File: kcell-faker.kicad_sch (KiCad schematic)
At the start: 22 parts, among them J4 DBG, SW1 BOOT, SW2 RST, SW3 UP, SW4 DOWN, SW5 RANGE, U6 ESP32-S3-MINI-1

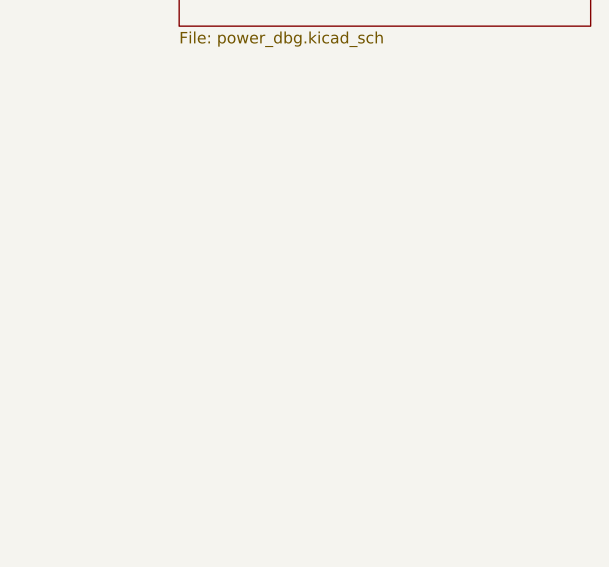
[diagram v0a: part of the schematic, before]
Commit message: Add logos and mounting holes
Straighen up some stuff, align better, untangle transistor outputs
Should we add pins for teh spare channels? we have the ios?
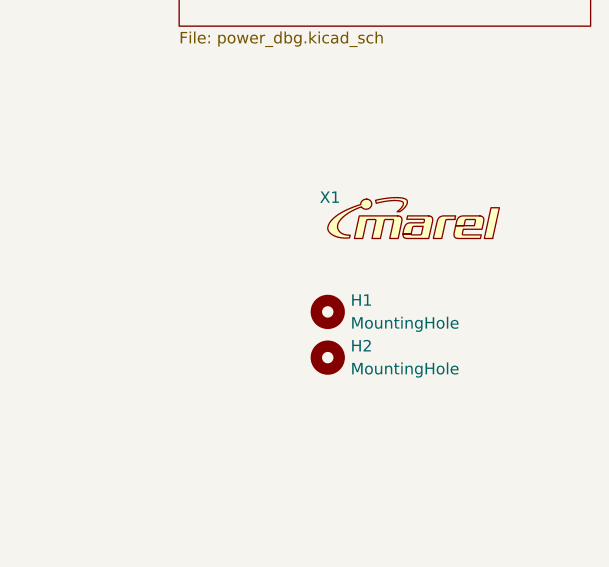
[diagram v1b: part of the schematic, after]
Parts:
- added H1, H2: MountingHole, MountingHole:MountingHole_3.2mm_M3, symbol Mechanical:MountingHole
- added X1: ~, marel-footprints:Logo_Marel_5.3x1.1mm, symbol karl-atomic-basic:Logo_Marel
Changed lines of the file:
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@@
+	)
+	(symbol
+		(lib_id "karl-atomic-basic:Logo_Marel")
+		(at 246.38 129.54 0)
+		(unit 1)
+		(exclude_from_sim no)
+		(in_bom no)
+		(on_board yes)
+		(dnp no)
+		(property "Reference" "X1"
+			(at 246.634 129.54 0)
+			(effects
+				(font
+					(size 1.27 1.27)
+				)
+			)
+		)
+		(property "Value" "~"
+			(at 249.5583 128.27 0)
+			(effects
+				(font
+					(size 1.27 1.27)
+				)
+			)
+		)
+		(property "Footprint" "marel-footprints:Logo_Marel_5.3x1.1mm"
+			(at 246.38 129.54 0)
+			(effects
+				(font
+					(size 1.27 1.27)
+				)
+				(hide yes)
+			)
+		)
+		(property "Datasheet" ""
+			(at 246.38 129.54 0)
+			(effects
+				(font
+					(size 1.27 1.27)
+				)
+				(hide yes)
+			)
+		)
+		(property "Description" ""
+			(at 246.38 129.54 0)
+			(effects
+				(font
+					(size 1.27 1.27)
+				)
+				(hide yes)
+			)
+		)
+		(instances
+			(project ""
+				(path "/dc836b5d-e5fb-485d-8f74-ab331e55e69f"
+					(reference "X1")
+					(unit 1)
+				)
+			)
+		)
 	)
 	(symbol
@@
 	)
 	(symbol
+		(lib_id "Mechanical:MountingHole")
+		(at 246.38 147.32 0)
+		(unit 1)
+		(exclude_from_sim yes)
+		(in_bom no)
+		(on_board yes)
+		(dnp no)
+		(fields_autoplaced yes)
+		(property "Reference" "H2"
+			(at 248.92 146.0499 0)
+			(effects
+				(font
+					(size 1.27 1.27)
+				)
+				(justify left)
+			)
+		)
+		(property "Value" "MountingHole"
+			(at 248.92 148.5899 0)
+			(effects
+				(font
+					(size 1.27 1.27)
+				)
+				(justify left)
+			)
+		)
+		(property "Footprint" "MountingHole:MountingHole_3.2mm_M3"
+			(at 246.38 147.32 0)
+			(effects
+				(font
+					(size 1.27 1.27)
+				)
+				(hide yes)
+			)
+		)
+		(property "Datasheet" "~"
+			(at 246.38 147.32 0)
+			(effects
+				(font
+					(size 1.27 1.27)
+				)
+				(hide yes)
+			)
+		)
+		(property "Description" "Mounting Hole without connection"
+			(at 246.38 147.32 0)
+			(effects
+				(font
+					(size 1.27 1.27)
+				)
+				(hide yes)
+			)
+		)
+		(instances
+			(project "kcell-faker"
+				(path "/dc836b5d-e5fb-485d-8f74-ab331e55e69f"
+					(reference "H2")
+					(unit 1)
+				)
+			)
+		)
+	)
+	(symbol
 		(lib_id "Device:LED_Small")
 		(at 48.26 170.18 90)
@@
 					(unit 1)
 				)
+			)
+		)
+	)
+	(symbol
+		(lib_id "Mechanical:MountingHole")
+		(at 246.38 142.24 0)
+		(unit 1)
+		(exclude_from_sim yes)
+		(in_bom no)
+		(on_board yes)
+		(dnp no)
+		(fields_autoplaced yes)
+		(property "Reference" "H1"
+			(at 248.92 140.9699 0)
+			(effects
+				(font
+					(size 1.27 1.27)
+				)
+				(justify left)
+			)
+		)
+		(property "Value" "MountingHole"
+			(at 248.92 143.5099 0)
+			(effects
+				(font
+					(size 1.27 1.27)
+				)
+				(justify left)
+			)
+		)
+		(property "Footprint" "MountingHole:MountingHole_3.2mm_M3"
+			(at 246.38 142.24 0)
+			(effects
+				(font
+					(size 1.27 1.27)
+				)
+				(hide yes)
+			)
+		)
+		(property "Datasheet" "~"
+			(at 246.38 142.24 0)
+			(effects
+				(font
+					(size 1.27 1.27)
+				)
+				(hide yes)
+			)
+		)
+		(property "Description" "Mounting Hole without connection"
+			(at 246.38 142.24 0)
+			(effects
+				(font
+					(size 1.27 1.27)
+				)
+				(hide yes)
+			)
+		)
+		(instances
+			(project ""
+				(path "/dc836b5d-e5fb-485d-8f74-ab331e55e69f"
+					(reference "H1")
+					(unit 1)
+				)

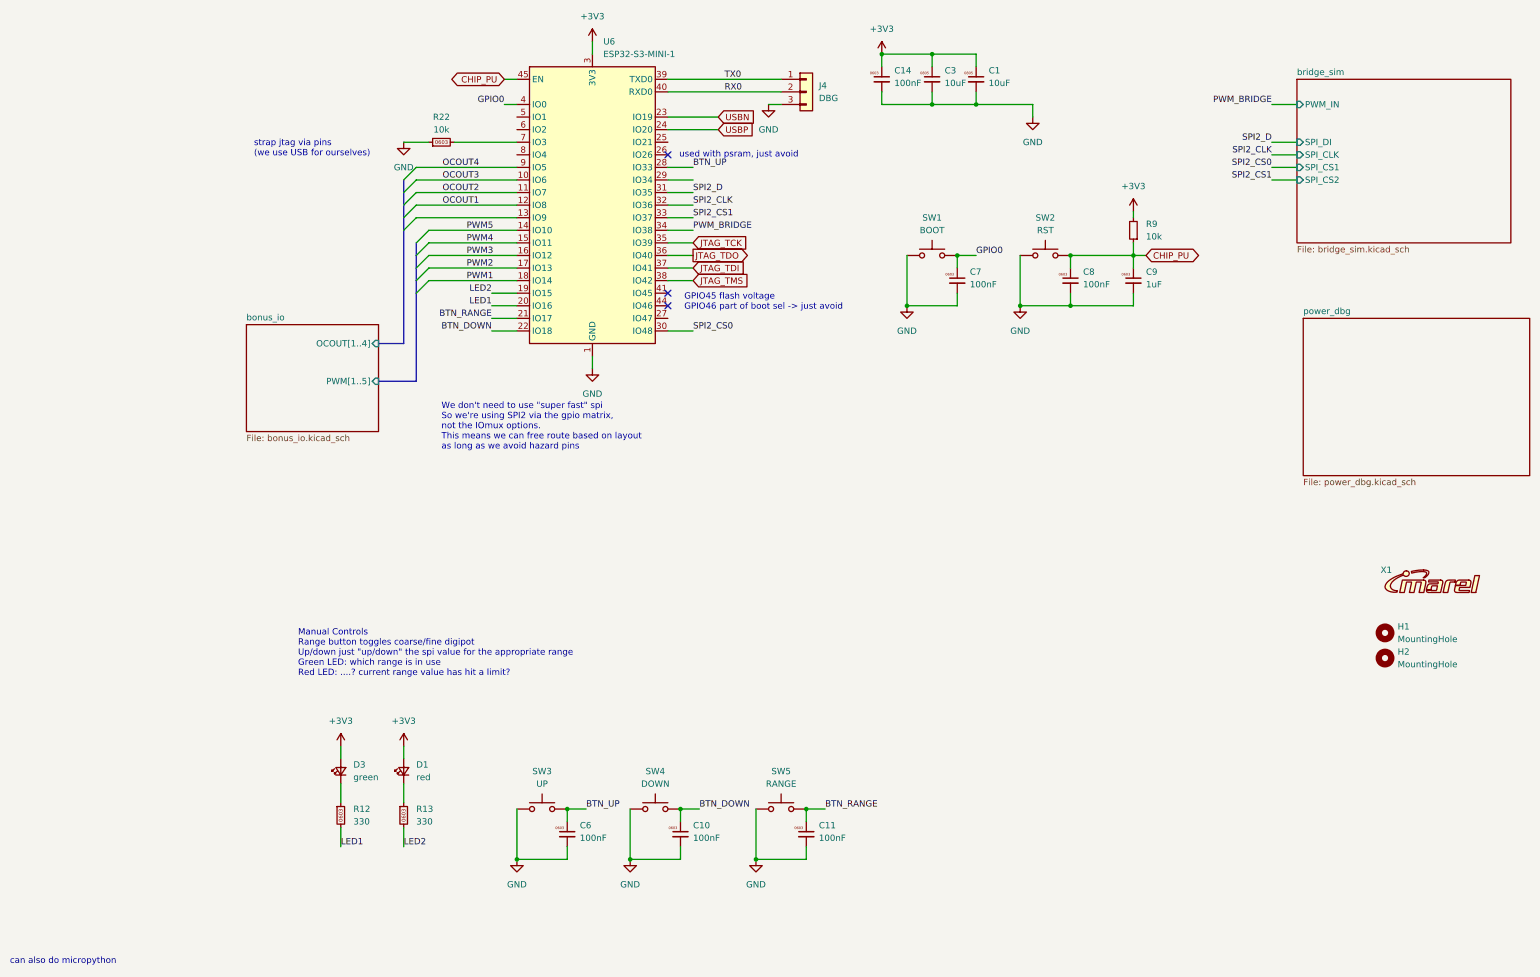
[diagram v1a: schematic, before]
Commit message: erc, board stackup
board stackup for jlc 7628, for 90 ohm usb. netclasses added, but not
connected. erc started, fixed up more grid issues, pushed some more text
and added the basic power islands
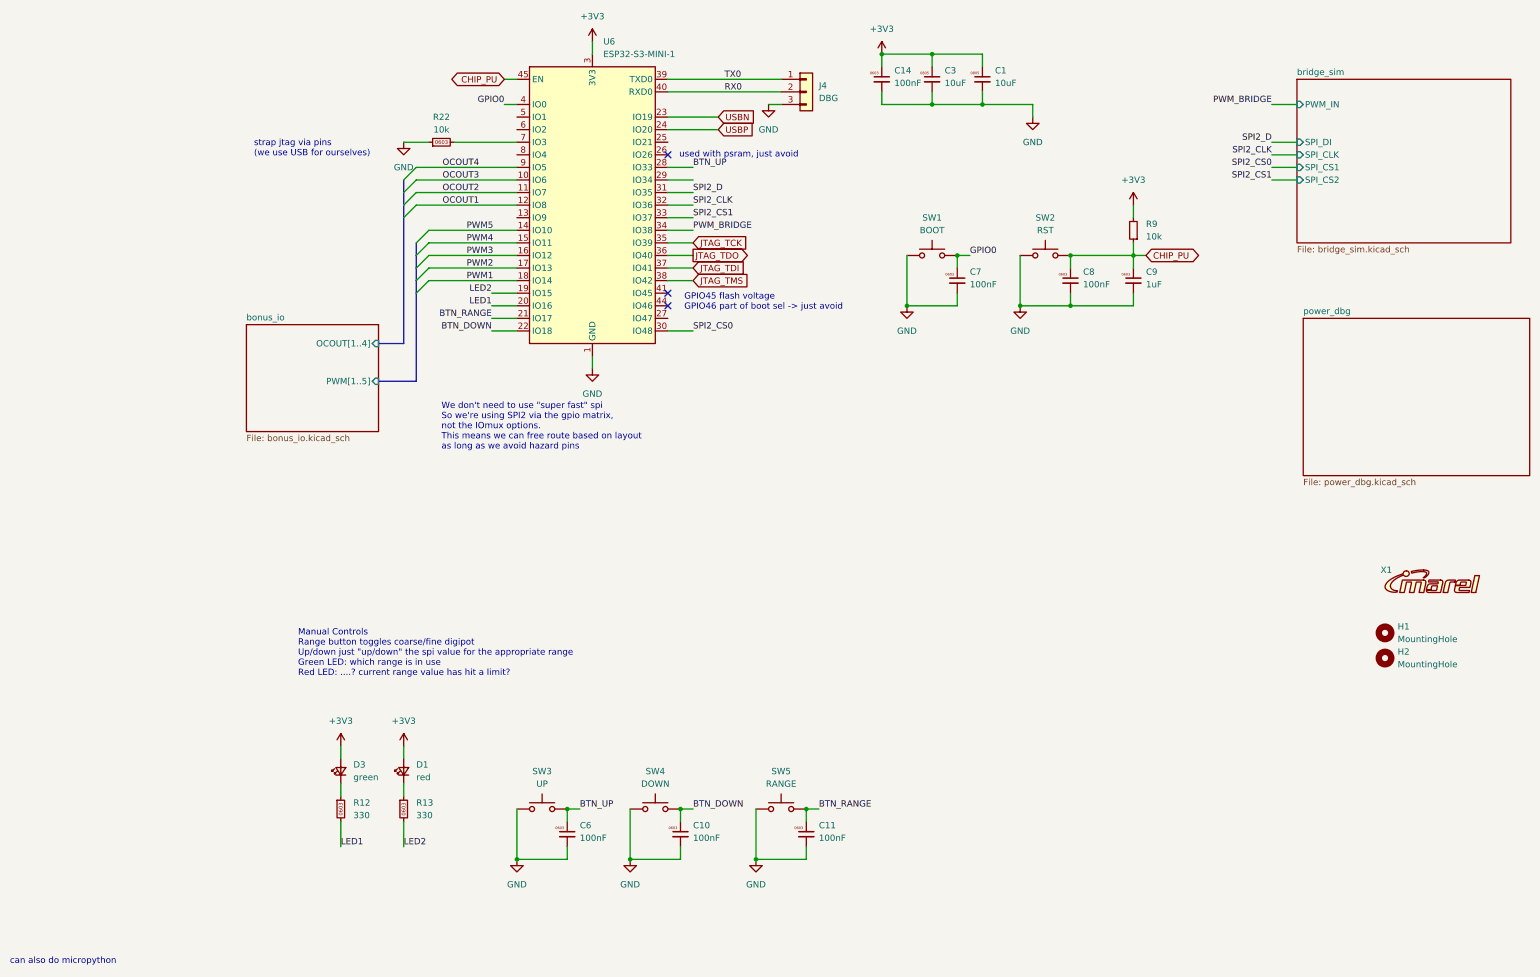
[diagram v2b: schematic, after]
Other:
- moved on the sheet: C1, R12, R13
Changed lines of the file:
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@@
 	)
 	(junction
-		(at 163.83 35.56)
+		(at 104.14 177.8)
 		(diameter 0)
 		(color 0 0 0 0)
 	)
 	(junction
-		(at 104.14 177.8)
+		(at 71.12 187.96)
 		(diameter 0)
 		(color 0 0 0 0)
 	)
 	(junction
-		(at 71.12 187.96)
+		(at 195.58 66.04)
 		(diameter 0)
 		(color 0 0 0 0)
 	)
 	(junction
-		(at 195.58 66.04)
+		(at 165.1 35.56)
 		(diameter 0)
 		(color 0 0 0 0)
@@
 	)
 	(bus_entry
-		(at 50.8 58.42)
-		(size -2.54 2.54)
-		(stroke
-			(width 0)
-			(type default)
-		)
-	)
-	(bus_entry
 		(at 50.8 73.66)
 		(size 2.54 -2.54)
@@
 		)
 	)
-	(bus
-		(pts
-			(xy 48.26 58.42) (xy 48.26 60.96)
-		)
-		(stroke
-			(width 0)
-			(type default)
-		)
-	)
 	(wire
 		(pts
@@
 	(wire
 		(pts
-			(xy 129.54 177.8) (xy 133.35 177.8)
+			(xy 129.54 177.8) (xy 132.08 177.8)
 		)
 		(stroke
@@
 	(wire
 		(pts
-			(xy 35.56 172.72) (xy 35.56 176.53)
+			(xy 35.56 172.72) (xy 35.56 175.26)
 		)
 		(stroke
@@
 	(wire
 		(pts
-			(xy 160.02 66.04) (xy 163.83 66.04)
+			(xy 160.02 66.04) (xy 162.56 66.04)
 		)
 		(stroke
@@
 	(wire
 		(pts
-			(xy 195.58 57.15) (xy 195.58 58.42)
+			(xy 195.58 55.88) (xy 195.58 58.42)
 		)
 		(stroke
@@
 	(wire
 		(pts
-			(xy 48.26 172.72) (xy 48.26 176.53)
+			(xy 48.26 172.72) (xy 48.26 175.26)
 		)
 		(stroke
@@
 	(wire
 		(pts
-			(xy 154.94 35.56) (xy 163.83 35.56)
+			(xy 154.94 35.56) (xy 165.1 35.56)
 		)
 		(stroke
@@
 	(wire
 		(pts
-			(xy 163.83 33.02) (xy 163.83 35.56)
+			(xy 165.1 33.02) (xy 165.1 35.56)
 		)
 		(stroke
@@
 	(wire
 		(pts
-			(xy 154.94 25.4) (xy 163.83 25.4)
+			(xy 154.94 25.4) (xy 165.1 25.4)
 		)
 		(stroke
@@
 	(wire
 		(pts
-			(xy 35.56 181.61) (xy 35.56 185.42)
+			(xy 35.56 180.34) (xy 35.56 185.42)
 		)
 		(stroke
@@
 	(wire
 		(pts
-			(xy 50.8 58.42) (xy 71.12 58.42)
-		)
-		(stroke
-			(width 0)
-			(type default)
-		)
-	)
-	(wire
-		(pts
 			(xy 182.88 73.66) (xy 182.88 76.2)
 		)
@@
 	(wire
 		(pts
-			(xy 81.28 177.8) (xy 85.09 177.8)
+			(xy 81.28 177.8) (xy 83.82 177.8)
 		)
 		(stroke
@@
 	(bus
 		(pts
-			(xy 48.26 60.96) (xy 48.26 83.82)
+			(xy 48.26 58.42) (xy 48.26 83.82)
 		)
 		(stroke
@@
 	(wire
 		(pts
-			(xy 48.26 181.61) (xy 48.26 185.42)
+			(xy 48.26 180.34) (xy 48.26 185.42)
 		)
 		(stroke
@@
 	(wire
 		(pts
-			(xy 104.14 177.8) (xy 107.95 177.8)
+			(xy 104.14 177.8) (xy 106.68 177.8)
 		)
 		(stroke
@@
 	(wire
 		(pts
-			(xy 163.83 35.56) (xy 175.26 35.56)
+			(xy 165.1 35.56) (xy 175.26 35.56)
 		)
 		(stroke
@@
 	(wire
 		(pts
-			(xy 163.83 27.94) (xy 163.83 25.4)
+			(xy 165.1 27.94) (xy 165.1 25.4)
 		)
 		(stroke
@@
 	)
 	(label "BTN_UP"
-		(at 85.09 177.8 0)
+		(at 83.82 177.8 0)
 		(fields_autoplaced yes)
 		(effects
@@
 	)
 	(label "BTN_DOWN"
-		(at 107.95 177.8 0)
+		(at 106.68 177.8 0)
 		(fields_autoplaced yes)
 		(effects
@@
 	)
 	(label "BTN_RANGE"
-		(at 133.35 177.8 0)
+		(at 132.08 177.8 0)
 		(fields_autoplaced yes)
 		(effects
@@
 	)
 	(label "GPIO0"
-		(at 163.83 66.04 0)
+		(at 162.56 66.04 0)
 		(fields_autoplaced yes)
 		(effects
@@
 	(symbol
 		(lib_id "karl-atomic-basic:KR0603_330R")
-		(at 35.56 179.07 0)
+		(at 35.56 177.8 0)
 		(unit 1)
 		(exclude_from_sim no)
@@
 		(fields_autoplaced yes)
 		(property "Reference" "R12"
-			(at 38.1 177.7999 0)
+			(at 38.1 176.5299 0)
 			(effects
 				(font
@@
 		)
 		(property "Value" "330"
-			(at 38.1 180.3399 0)
+			(at 38.1 179.0699 0)
 			(effects
 				(font
@@
 		)
 		(property "Footprint" "Resistor_SMD:R_0603_1608Metric"
-			(at 35.56 179.07 0)
+			(at 35.56 177.8 0)
 			(effects
 				(font
@@
 		)
 		(property "Datasheet" "~"
-			(at 35.56 179.07 0)
+			(at 35.56 177.8 0)
 			(effects
 				(font
@@
 		)
 		(property "Description" "Resistor, 0603"
-			(at 35.56 179.07 0)
+			(at 35.56 177.8 0)
 			(effects
 				(font
@@
 		)
 		(property "MPN" "0603WAF3300T5E"
-			(at 35.56 179.07 0)
+			(at 35.56 177.8 0)
 			(effects
 				(font
@@
 		)
 		(property "LCSC Part#" "C23138"
-			(at 35.56 179.07 0)
+			(at 35.56 177.8 0)
 			(effects
 				(font
@@
 	(symbol
 		(lib_id "karl-atomic-basic:KC0805_10uF_25V")
-		(at 163.83 30.48 0)
+		(at 165.1 30.48 0)
 		(unit 1)
 		(exclude_from_sim no)
@@
 		(fields_autoplaced yes)
 		(property "Reference" "C1"
-			(at 166.37 28.7071 0)
+			(at 167.64 28.7071 0)
 			(effects
 				(font
@@
 		)
 		(property "Value" "10uF"
-			(at 166.37 31.2471 0)
+			(at 167.64 31.2471 0)
 			(effects
 				(font
@@
 		)
 		(property "Footprint" "Capacitor_SMD:C_0805_2012Metric"
-			(at 163.322 34.29 0)
+			(at 164.592 34.29 0)
 			(effects
 				(font
@@
 		)
 		(property "Datasheet" "~"
-			(at 163.83 30.48 0)
+			(at 165.1 30.48 0)
 			(effects
 				(font
@@
 		)
 		(property "Description" "25V, X5R"
-			(at 163.83 34.29 0)
+			(at 165.1 34.29 0)
 			(effects
 				(font
@@
 		)
 		(property "MPN" "CL21A106KAYNNNE"
-			(at 163.576 34.29 0)
+			(at 164.846 34.29 0)
 			(effects
 				(font
@@
 		)
 		(property "LCSC Part#" "C15850"
-			(at 163.83 34.29 0)
+			(at 165.1 34.29 0)
 			(effects
 				(font
@@
 	(symbol
 		(lib_id "karl-atomic-basic:KR0603_330R")
-		(at 48.26 179.07 0)
+		(at 48.26 177.8 0)
 		(unit 1)
 		(exclude_from_sim no)
@@
 		(fields_autoplaced yes)
 		(property "Reference" "R13"
-			(at 50.8 177.7999 0)
+			(at 50.8 176.5299 0)
 			(effects
 				(font
@@
 		)
 		(property "Value" "330"
-			(at 50.8 180.3399 0)
+			(at 50.8 179.0699 0)
 			(effects
 				(font
@@
 		)
 		(property "Footprint" "Resistor_SMD:R_0603_1608Metric"
-			(at 48.26 179.07 0)
+			(at 48.26 177.8 0)
 			(effects
 				(font
@@
 		)
 		(property "Datasheet" "~"
-			(at 48.26 179.07 0)
+			(at 48.26 177.8 0)
 			(effects
 				(font
@@
 		)
 		(property "Description" "Resistor, 0603"
-			(at 48.26 179.07 0)
+			(at 48.26 177.8 0)
 			(effects
 				(font
@@
 		)
 		(property "MPN" "0603WAF3300T5E"
-			(at 48.26 179.07 0)
+			(at 48.26 177.8 0)
 			(effects
 				(font
@@
 		)
 		(property "LCSC Part#" "C23138"
-			(at 48.26 179.07 0)
+			(at 48.26 177.8 0)
 			(effects
 				(font
@@
 	(symbol
 		(lib_id "power:+3V3")
-		(at 195.58 57.15 0)
+		(at 195.58 55.88 0)
 		(unit 1)
 		(exclude_from_sim no)
@@
 		(fields_autoplaced yes)
 		(property "Reference" "#PWR09"
-			(at 195.58 60.96 0)
+			(at 195.58 59.69 0)
 			(effects
 				(font
@@
 		)
 		(property "Value" "+3V3"
-			(at 195.58 52.07 0)
+			(at 195.58 50.8 0)
 			(effects
 				(font
@@
 		)
 		(property "Footprint" ""
-			(at 195.58 57.15 0)
+			(at 195.58 55.88 0)
 			(effects
 				(font
@@
 		)
 		(property "Datasheet" ""
-			(at 195.58 57.15 0)
+			(at 195.58 55.88 0)
 			(effects
 				(font
@@
 		)
 		(property "Description" "Power symbol creates a global label with name \"+3V3\""
-			(at 195.58 57.15 0)
+			(at 195.58 55.88 0)
 			(effects
 				(font

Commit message: quick route stab
do we want to have a better jumper option for gpio3? yes?
add silk for version, source, description
review last expansion options (pins for ulnx outputs? silk for jtag,
silk for ...?
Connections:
- net BTN_DOWN: now also U6.19 (IO15); no longer U6.22 (IO18)
- net BTN_RANGE: now also U6.20 (IO16); no longer U6.21 (IO17)
- net LED1: now also U6.27 (IO47); no longer U6.20 (IO16)
- net LED2: now also U6.21 (IO17); no longer U6.19 (IO15)
- net SPI2_CLK: now also U6.30 (IO48); no longer U6.32 (IO36)
- net SPI2_CS0: now also U6.32 (IO36); no longer U6.30 (IO48)
- net SPI2_D: now also U6.29 (IO34); no longer U6.31 (IO35)
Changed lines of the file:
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@@
+	(wire
+		(pts
+			(xy 106.68 78.74) (xy 101.6 78.74)
+		)
+		(stroke
+			(width 0)
+			(type default)
+		)
+	)
 	(wire
 		(pts
@@
 	)
 	(label "SPI2_CS0"
-		(at 106.68 81.28 0)
+		(at 106.68 55.88 0)
 		(fields_autoplaced yes)
 		(effects
@@
 	)
 	(label "BTN_RANGE"
-		(at 66.04 78.74 180)
+		(at 66.04 76.2 180)
 		(fields_autoplaced yes)
 		(effects
@@
 	)
 	(label "LED1"
-		(at 66.04 76.2 180)
-		(fields_autoplaced yes)
-		(effects
-			(font
-				(size 1.27 1.27)
-			)
-			(justify right bottom)
+		(at 106.68 78.74 0)
+		(fields_autoplaced yes)
+		(effects
+			(font
+				(size 1.27 1.27)
+			)
+			(justify left bottom)
 		)
 	)
 	(label "BTN_DOWN"
-		(at 66.04 81.28 180)
+		(at 66.04 73.66 180)
 		(fields_autoplaced yes)
 		(effects
@@
 	)
 	(label "LED2"
-		(at 66.04 73.66 180)
+		(at 66.04 78.74 180)
 		(fields_autoplaced yes)
 		(effects
@@
 	)
 	(label "SPI2_D"
-		(at 106.68 53.34 0)
+		(at 106.68 50.8 0)
 		(fields_autoplaced yes)
 		(effects
@@
 	)
 	(label "SPI2_CLK"
-		(at 106.68 55.88 0)
-		(fields_autoplaced yes)
-		(effects
+		(at 106.68 81.28 0)
+		(fields_autoplaced yes)
+		(effects

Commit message: "final" rev1?
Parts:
- added R19: 510R, Resistor_SMD:R_0603_1608Metric, symbol karl-atomic-basic:KR0603_510R
- added R20: 10k, Resistor_SMD:R_0603_1608Metric, symbol karl-atomic-basic:KR0603_10k
- D3: MPN KT-0805G -> KT-0805G
- X1: footprint marel-footprints:Logo_Marel_5.3x1.1mm -> marel-footprints:Logo_Marel_5.3x1.1mm_copper
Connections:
- net +3V3: now also R20.1
- net TX0: now also R19.2; no longer U6.39 (TXD0)
- net at R22.2, U6.7 (IO3): now also R20.2
- new net: R19.1, U6.39 (TXD0)
